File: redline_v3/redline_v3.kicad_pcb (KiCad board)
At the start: 2 copper layers, 89.1 x 94.5 mm, 67 parts, among them J1 Conn_01x10_Socket, J2 Conn_01x10_Socket

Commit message: V3 with Gia layout
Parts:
- moved D23 79.7 mm to (218.7, 137.6), turned to 90 degrees
- moved D33 73.0 mm to (216.6, 137.5), turned to 90 degrees
- moved D24 71.7 mm to (213.9, 133.2), turned to 90 degrees
- moved J2 71.1 mm to (232.4, 101.7), turned to 0 degrees
- moved D17 66.1 mm to (170.4, 67.9), turned to 0 degrees
- moved D12 66.1 mm to (190.6, 91.4), turned to -90 degrees
- moved D11 65.6 mm to (185.7, 86.6), turned to 0 degrees
- moved D21 65.5 mm to (185.7, 84.7)
- moved D22 65.2 mm to (192.6, 91.4), turned to -90 degrees
- moved D34 64.9 mm to (211.6, 133.2), turned to 90 degrees
- moved D1 63.9 mm to (155.1, 134.1)
- moved D2 63.7 mm to (155.0, 135.9)
- moved D18 61.2 mm to (174.1, 72.5), turned to 0 degrees
- moved D42 59.1 mm to (190.5, 94.9), turned to 90 degrees
- moved D7 58.7 mm to (170.4, 69.8), turned to 0 degrees
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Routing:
- net /1: track 0.00 -> 211.9 mm
- net /0: track 39.0 -> 236.2 mm
- net /2: track 0.00 -> 103.5 mm
- net /3: track 0.00 -> 88.5 mm
- net Net-(D1-K): track 57.1 -> 0.00 mm
- net /8: track 0.00 -> 32.9 mm
- net /9: track 39.2 -> 8.06 mm
- net /5: track 44.0 -> 73.3 mm
- net Net-(D10-K): track 28.8 -> 0.00 mm
- net Net-(D43-K): track 4.46 -> 31.8 mm
- net Net-(D23-K): track 35.0 -> 8.78 mm, vias 4 -> 0
- net /4: track 41.5 -> 65.3 mm
- net /6: track 55.0 -> 76.3 mm
- net /7: track 37.4 -> 55.5 mm
- net Net-(D33-K): track 4.57 -> 17.8 mm
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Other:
- board size 89.1 x 94.5 mm -> 104.8 x 108.8 mm

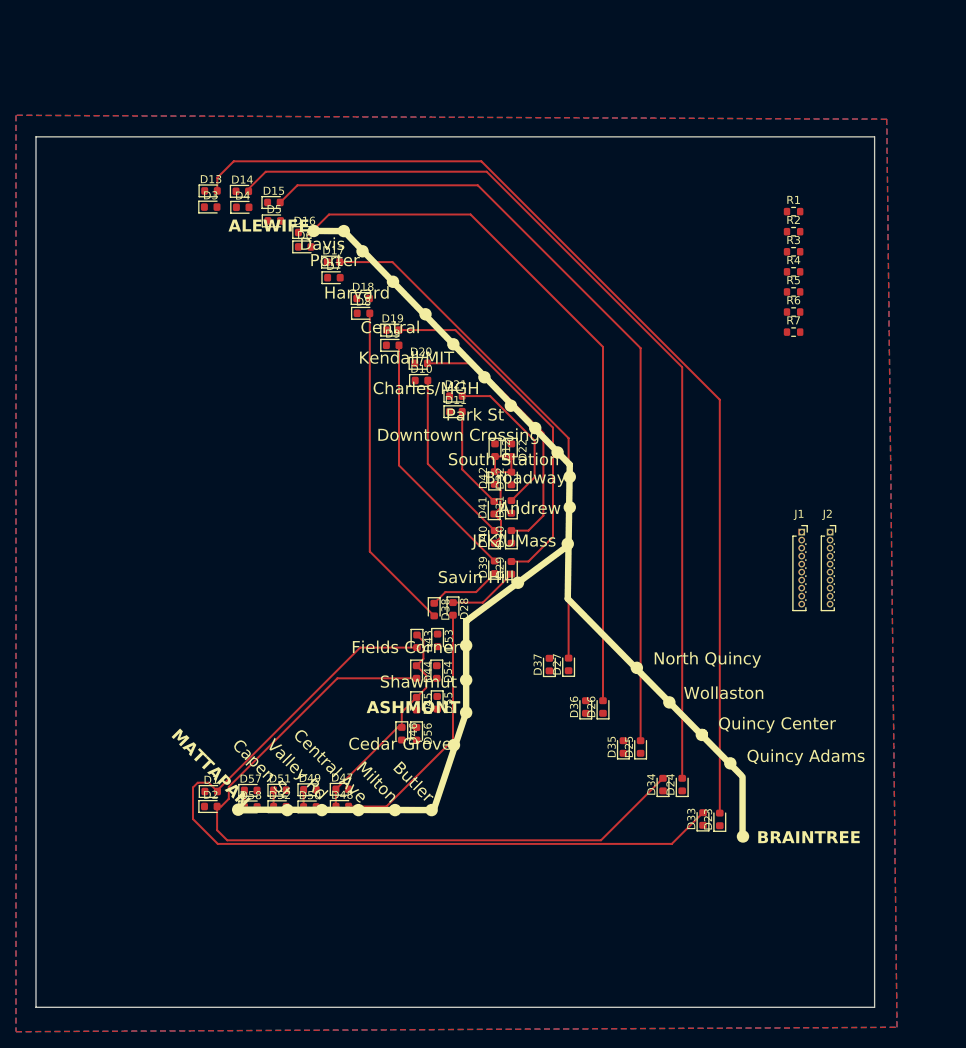
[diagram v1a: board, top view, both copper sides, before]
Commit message: remove old silkscreen
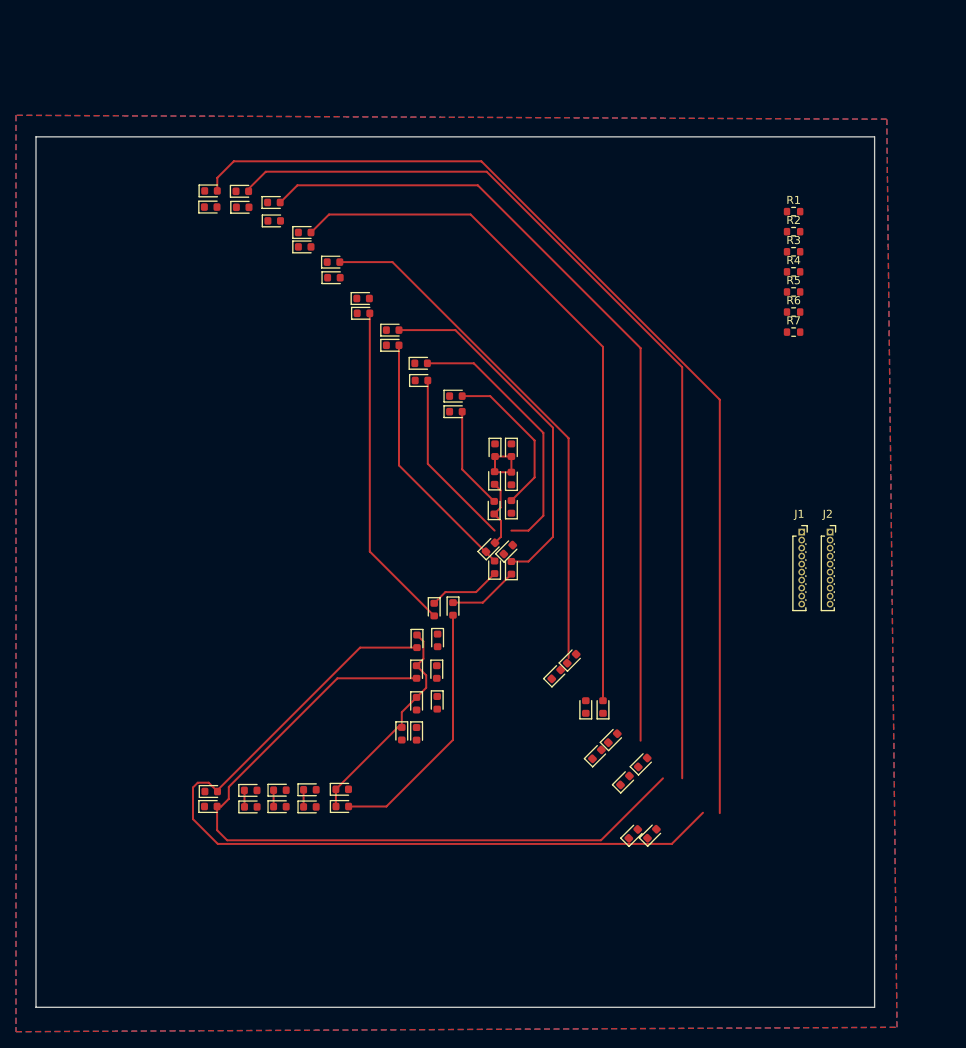
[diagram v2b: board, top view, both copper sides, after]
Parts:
- moved D33 8.91 mm to (207.8, 139.4), turned to 45 degrees
- moved D23 8.67 mm to (210.2, 139.4), turned to 45 degrees
- moved D24 5.66 mm to (209.0, 130.4), turned to 45 degrees
- moved D34 4.78 mm to (206.8, 132.7), turned to 45 degrees
- moved D25 3.65 mm to (205.3, 127.4), turned to 45 degrees
- moved D35 3.43 mm to (203.3, 129.4), turned to 45 degrees
- moved D30 1.63 mm to (192.2, 103.8), turned to 45 degrees
- moved D37 1.49 mm to (198.2, 119.4), turned to 45 degrees
- moved D40 1.39 mm to (190.0, 103.5), turned to 45 degrees
- moved D27 0.81 mm to (200.1, 117.5), turned to 45 degrees
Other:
- board text removed: "ALEWIFE"
- board text removed: "ASHMONT"
- board text removed: "Andrew"
- board text removed: "BRAINTREE"
- board text removed: "Broadway"
- board text removed: "Butler"
- board text removed: "Capen St"
- board text removed: "Cedar Grove"
- board text removed: "Central"
- board text removed: "Central Ave"
- board text removed: "Charles/MGH"
- board text removed: "Davis"
- board text removed: "Downtown Crossing"
- board text removed: "Fields Corner"
- board text removed: "Harvard"
- board text removed: "JFK/UMass"
- board text removed: "Kendall/MIT"
- board text removed: "MATTAPAN"
- board text removed: "Milton"
- board text removed: "North Quincy"
- board text removed: "Park St"
- board text removed: "Porter"
- board text removed: "Quincy Adams"
- board text removed: "Quincy Center"
- board text removed: "Savin Hill"
- board text removed: "Shawmut"
- board text removed: "South Station"
- board text removed: "Valley Rd"
- board text removed: "Wollaston"

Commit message: fix led locations
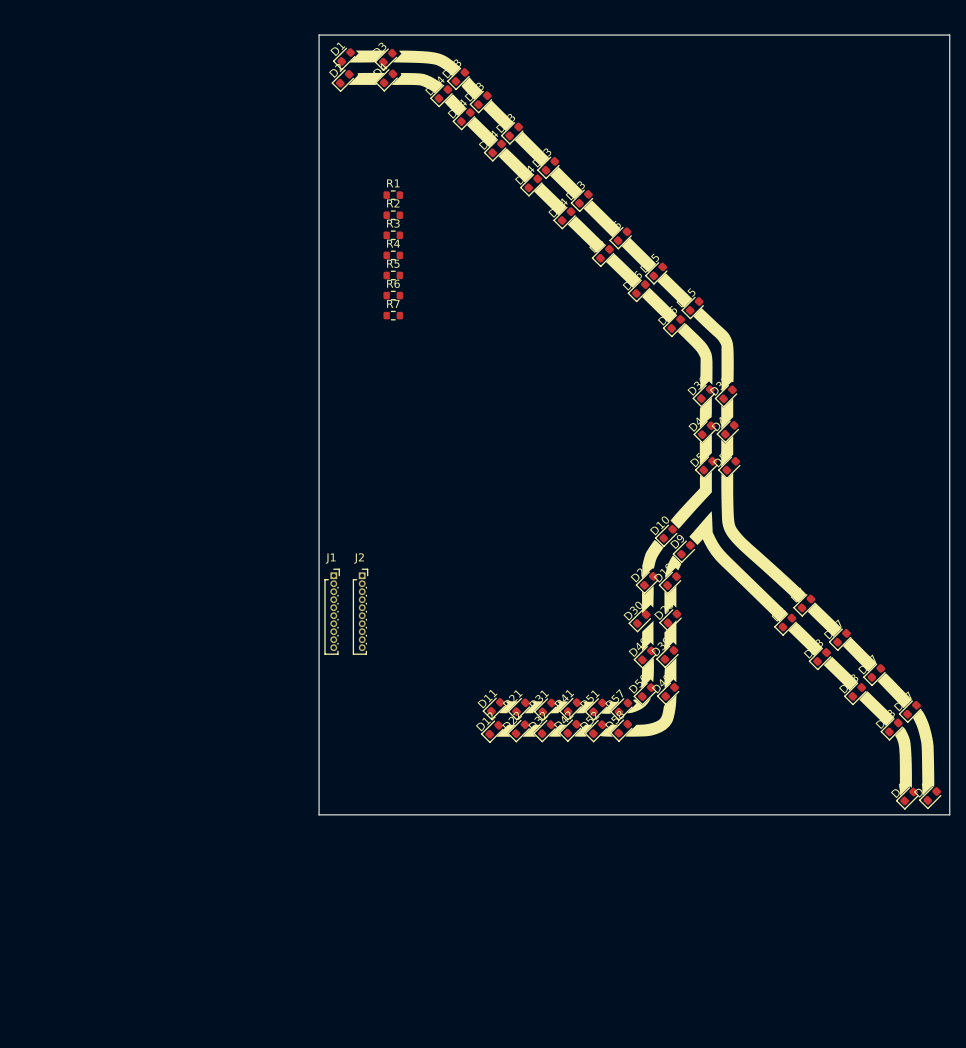
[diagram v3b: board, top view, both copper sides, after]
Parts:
- added G***: LOGO, silkscreen:redline_nolabels, F.Cu at (209.2, 87.9)
- moved D23 94.1 mm to (189.0, 47.7)
- moved D1 93.4 mm to (171.9, 42.3), turned to 45 degrees
- moved D2 92.5 mm to (171.8, 45.0), turned to 45 degrees
- moved D33 89.1 mm to (192.9, 51.6)
- moved D24 83.6 mm to (186.9, 49.8)
- moved D34 80.6 mm to (190.8, 53.7)
- moved D17 79.0 mm to (233.9, 114.9), turned to 45 degrees
- moved D47 73.8 mm to (245.2, 134.6), turned to 45 degrees
- moved D18 72.8 mm to (231.4, 117.3), turned to 45 degrees
- moved D7 71.8 mm to (229.5, 110.6), turned to 45 degrees
- moved D48 70.9 mm to (242.3, 134.7), turned to 45 degrees
- moved D8 65.6 mm to (227.1, 113.0), turned to 45 degrees
- moved D44 62.8 mm to (195.3, 58.1), turned to 45 degrees
- moved D43 61.7 mm to (197.5, 55.9), turned to 45 degrees
- moved D38 59.3 mm to (240.4, 126.1), turned to 45 degrees
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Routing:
- net /0: track 236.2 -> 0.00 mm
- net /1: track 211.9 -> 0.00 mm
- net /2: track 103.5 -> 0.00 mm
- net /3: track 88.5 -> 0.00 mm
- net /6: track 76.3 -> 0.00 mm
- net /5: track 73.3 -> 0.00 mm
- net /4: track 65.3 -> 0.00 mm
- net /7: track 55.5 -> 0.00 mm
- net /8: track 32.9 -> 0.00 mm
- net Net-(D43-K): track 31.8 -> 0.00 mm
- net Net-(D33-K): track 17.8 -> 0.00 mm
- net Net-(D23-K): track 8.78 -> 0.00 mm
- net /9: track 8.06 -> 0.00 mm
- net Net-(D53-K): track 2.07 -> 0.00 mm
- removed copper zone on B.Cu, net GND
- removed copper zone on F.Cu, net GND
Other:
- board size 104.8 x 108.8 mm -> 78.8 x 97.5 mm

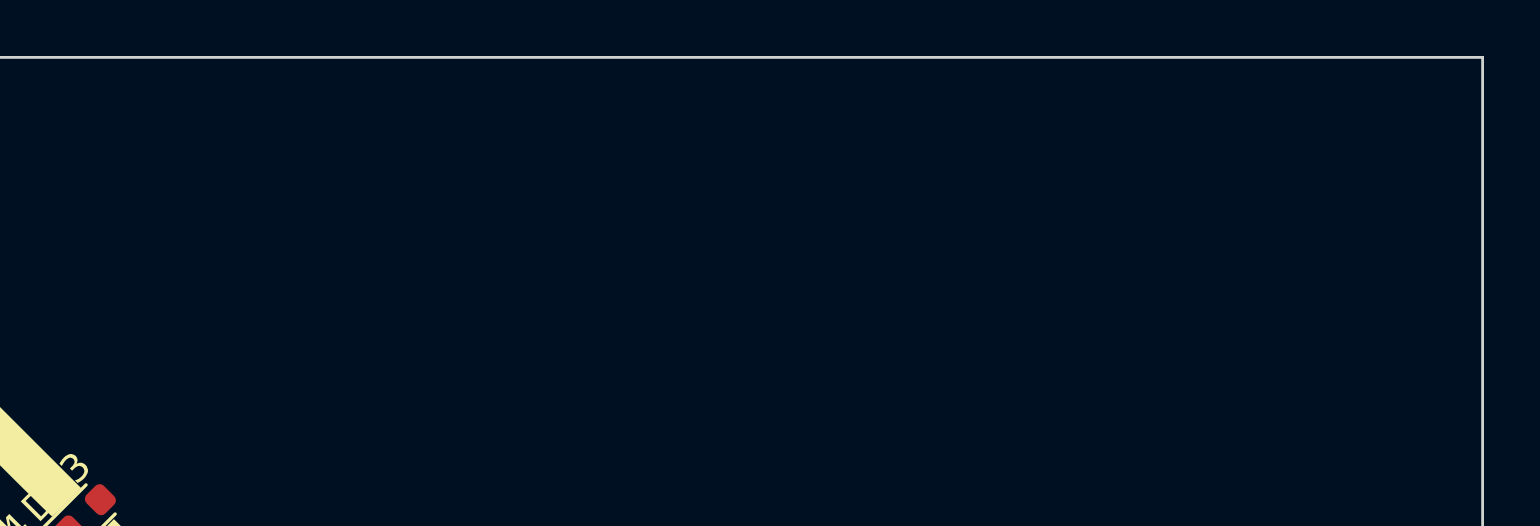
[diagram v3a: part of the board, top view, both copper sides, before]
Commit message: add mbta sign
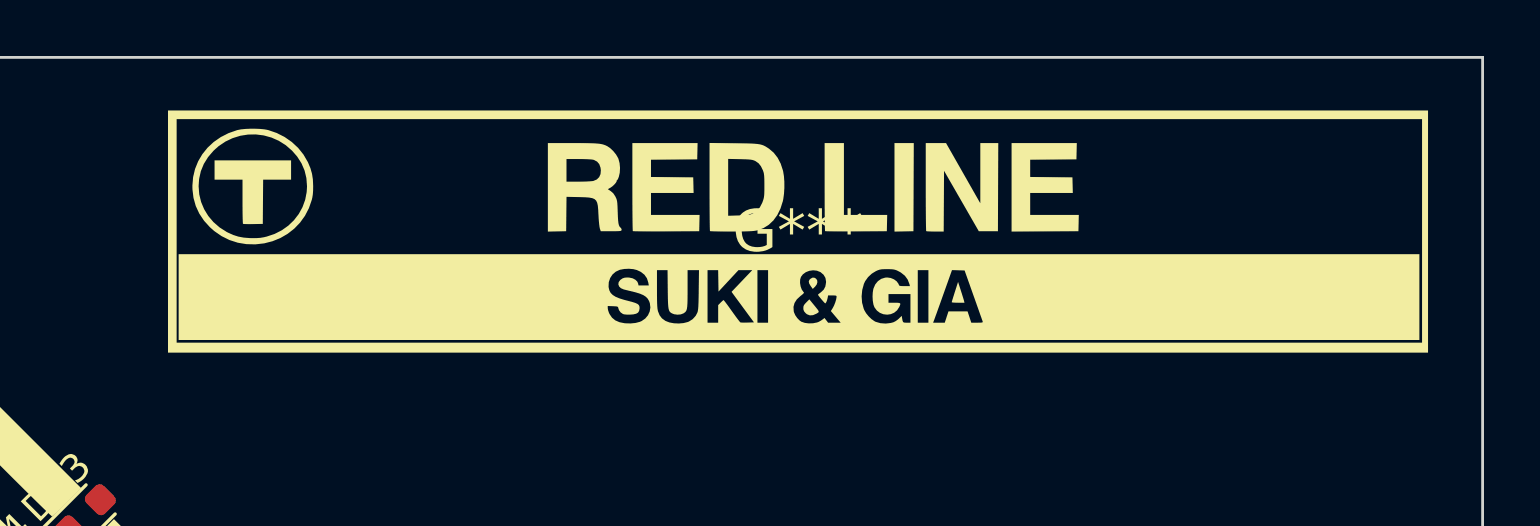
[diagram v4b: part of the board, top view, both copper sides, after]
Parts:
- added G***: LOGO, silkscreen:sign, F.Cu at (222.9, 45.7)

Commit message: traces all done
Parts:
- removed the G*** at (222.9, 45.7)
- removed J1, J2: Conn_01x10_Socket, Connector_PinSocket_1.00mm:PinSocket_1x10_P1.00mm_Vertical
- added C1: 10nF, Capacitor_SMD:C_0603_1608Metric, F.Cu at (220.5, 77.5)
- added C2: 3.3nF, Capacitor_SMD:C_0603_1608Metric, F.Cu at (223.0, 76.8)
- added C3: C_1uF, footprints:C_0603_1608Metric, F.Cu at (231.2, 82.8)
- added C4: C_1uF, footprints:C_0603_1608Metric, F.Cu at (227.7, 85.8)
- added J4: 48037-0001, custom_library:MOLEX_USB_conn, F.Cu at (216.2, 55.0)
- added R8: R_US, Resistor_SMD:R_0603_1608Metric, F.Cu at (223.1, 78.2)
- added U1: ESP32, Package_DFN_QFN:QFN-48-1EP_8x8mm_P0.5mm_EP6.2x6.2mm, F.Cu at (215.0, 81.5)
- added U2: MCP1702T-3302E_MB, custom_library:MCP1702T, F.Cu at (228.0, 82.8)
- moved D23 110.0 mm to (219.5, 153.3)
- moved D33 104.5 mm to (216.6, 153.3)
- moved D1 99.8 mm to (165.3, 141.8)
- moved D2 99.5 mm to (165.5, 144.3)
- moved D24 97.1 mm to (217.4, 142.0)
- moved D34 93.8 mm to (215.1, 144.3)
- moved R5 88.4 mm to (213.5, 150.5), turned to 90 degrees
- moved R1 81.7 mm to (161.5, 139.6), turned to 90 degrees
- moved D17 80.1 mm to (167.8, 69.6)
- moved D44 78.2 mm to (184.2, 135.4)
- moved R6 77.0 mm to (174.7, 149.0), turned to 180 degrees
- moved D43 76.1 mm to (184.1, 130.8)
- moved R7 74.9 mm to (169.0, 149.0), turned to 180 degrees
- moved D7 74.7 mm to (165.5, 71.9)
- moved D54 74.3 mm to (187.0, 135.4)
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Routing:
- net /1: track 0.00 -> 298.4 mm, vias 0 -> 15
- net /0: track 0.00 -> 284.1 mm, vias 0 -> 4
- net /2: track 0.00 -> 255.7 mm, vias 0 -> 11
- net /A: track 0.00 -> 188.6 mm, vias 0 -> 4
- net /4: track 0.00 -> 186.6 mm, vias 0 -> 11
- net /5: track 0.00 -> 175.5 mm, vias 0 -> 18
- net /3: track 0.00 -> 157.8 mm, vias 0 -> 11
- net /6: track 0.00 -> 150.6 mm, vias 0 -> 13
- net /G: track 0.00 -> 135.6 mm, vias 0 -> 2
- net /F: track 0.00 -> 130.4 mm, vias 0 -> 4
- net /7: track 0.00 -> 128.4 mm, vias 0 -> 12
- net /9: track 0.00 -> 120.0 mm, vias 0 -> 12
- net /8: track 0.00 -> 111.2 mm, vias 0 -> 8
- net /B: track 0.00 -> 104.3 mm, vias 0 -> 2
- net /E: track 0.00 -> 89.1 mm, vias 0 -> 2
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- added copper zone on B.Cu, net (none)
- added copper zone on F.Cu, net (none)
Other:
- board size 78.8 x 97.5 mm -> 104.8 x 108.8 mm

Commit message: add station names
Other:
- board text added: "Alewife"
- board text added: "Andrew"
- board text added: "Ashmont"
- board text added: "Braintree"
- board text added: "Broadway"
- board text added: "Butler"
- board text added: "Capen St"
- board text added: "Cedar Grove"
- board text added: "Central"
- board text added: "Central Ave"
- board text added: "Charles/MGH"
- board text added: "Davis"
- board text added: "Downtown Crossing"
- board text added: "Fields Corner"
- board text added: "Harvard"
- board text added: "JFK/UMass"
- board text added: "Kendall/MIT"
- board text added: "Mattapan"
- board text added: "Milton"
- board text added: "North Quincy"
- board text added: "Park St"
- board text added: "Porter"
- board text added: "Quincy Adams"
- board text added: "Quincy Center"
- board text added: "Savin Hill"
- board text added: "Shawmut"
- board text added: "South Station"
- board text added: "Valley Rd"
- board text added: "Wollaston"
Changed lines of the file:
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@@
   (gr_rect (start 133.175 52.243519) (end 238 161.05)
     (stroke (width 0.05) (type default)) (fill none) (layer "Edge.Cuts"))
+  (gr_text "Broadway" (at 195.93 103.45) (layer "F.SilkS")
+    (effects (font (size 1 1) (thickness 0.15)) (justify left bottom))
+  )
+  (gr_text "JFK/UMass" (at 195.77 112.49) (layer "F.SilkS")
+    (effects (font (size 1 1) (thickness 0.15)) (justify left bottom))
+  )
+  (gr_text "Mattapan\n" (at 164.89 147.11 -45) (layer "F.SilkS")
+    (effects (font (size 1 1) (thickness 0.15)) (justify left bottom))
+  )
+  (gr_text "Central Ave\n" (at 174.39 147.35 -45) (layer "F.SilkS")
+    (effects (font (size 1 1) (thickness 0.15)) (justify left bottom))
+  )
+  (gr_text "Charles/MGH" (at 177.46 77.14) (layer "F.SilkS")
+    (effects (font (size 1 1) (thickness 0.15)) (justify left bottom))
+  )
+  (gr_text "Valley Rd" (at 171.15 147.33 -45) (layer "F.SilkS")
+    (effects (font (size 1 1) (thickness 0.15)) (justify left bottom))
+  )
+  (gr_text "Butler\n" (at 180.83 147.32 -45) (layer "F.SilkS")
+    (effects (font (size 1 1) (thickness 0.15)) (justify left bottom))
+  )
+  (gr_text "Cedar Grove\n" (at 188.19 141.31 -45) (layer "F.SilkS")
+    (effects (font (size 1 1) (thickness 0.15)) (justify left bottom))
+  )
+  (gr_text "Fields Corner" (at 172.79 125.65) (layer "F.SilkS")
+    (effects (font (size 1 1) (thickness 0.15)) (justify left bottom))
+  )
+  (gr_text "North Quincy\n" (at 205.15 127.83) (layer "F.SilkS")
+    (effects (font (size 1 1) (thickness 0.15)) (justify left bottom))
+  )
+  (gr_text "Central" (at 168.87 68.54) (layer "F.SilkS")
+    (effects (font (size 1 1) (thickness 0.15)) (justify left bottom))
+  )
+  (gr_text "Wollaston\n" (at 209.62 132.06) (layer "F.SilkS")
+    (effects (font (size 1 1) (thickness 0.15)) (justify left bottom))
+  )
+  (gr_text "Park St" (at 182.12 81.98) (layer "F.SilkS")
+    (effects (font (size 1 1) (thickness 0.15)) (justify left bottom))
+  )
+  (gr_text "Andrew" (at 195.97 107.96) (layer "F.SilkS")
+    (effects (font (size 1 1) (thickness 0.15)) (justify left bottom))
+  )
+  (gr_text "Davis\n" (at 148.15 56.88 -45) (layer "F.SilkS")
+    (effects (font (size 1 1) (thickness 0.15)) (justify left bottom))
+  )
+  (gr_text "South Station" (at 191.11 90.69) (layer "F.SilkS")
+    (effects (font (size 1 1) (thickness 0.15)) (justify left bottom))
+  )
+  (gr_text "Downtown Crossing" (at 186.67 86.32) (layer "F.SilkS")
+    (effects (font (size 1 1) (thickness 0.15)) (justify left bottom))
+  )
+  (gr_text "Milton\n" (at 177.51 147.38 -45) (layer "F.SilkS")
+    (effects (font (size 1 1) (thickness 0.15)) (justify left bottom))
+  )
+  (gr_text "Quincy Center\n" (at 213.99 136.44) (layer "F.SilkS")
+    (effects (font (size 1 1) (thickness 0.15)) (justify left bottom))
+  )
+  (gr_text "Kendall/MIT" (at 173.19 73.08) (layer "F.SilkS")
+    (effects (font (size 1 1) (thickness 0.15)) (justify left bottom))
+  )
+  (gr_text "Braintree" (at 221.21 154.05) (layer "F.SilkS")
+    (effects (font (size 1 1) (thickness 0.15)) (justify left bottom))
+  )
+  (gr_text "Porter" (at 162.13 61.82) (layer "F.SilkS")
+    (effects (font (size 1 1) (thickness 0.15)) (justify left bottom))
+  )
+  (gr_text "Alewife" (at 141.5 56.16 -45) (layer "F.SilkS")
+    (effects (font (size 1 1) (thickness 0.15)) (justify left bottom))
+  )
+  (gr_text "Harvard" (at 165 64.64) (layer "F.SilkS")
+    (effects (font (size 1 1) (thickness 0.15)) (justify left bottom))
+  )
+  (gr_text "Savin Hill" (at 178.31 119.48) (layer "F.SilkS")
+    (effects (font (size 1 1) (thickness 0.15)) (justify left bottom))
+  )
+  (gr_text "Quincy Adams\n" (at 218.44 140.94) (layer "F.SilkS")
+    (effects (font (size 1 1) (thickness 0.15)) (justify left bottom))
+  )
+  (gr_text "Capen St" (at 167.86 147.35 -45) (layer "F.SilkS")
+    (effects (font (size 1 1) (thickness 0.15)) (justify left bottom))
+  )
+  (gr_text "Shawmut\n" (at 176.02 130.75) (layer "F.SilkS")
+    (effects (font (size 1 1) (thickness 0.15)) (justify left bottom))
+  )
+  (gr_text "Ashmont\n" (at 176.23 135.34) (layer "F.SilkS")
+    (effects (font (size 1 1) (thickness 0.15)) (justify left bottom))
+  )
   (segment (start 152.523694 60.036306) (end 153.636306 60.036306) (width 0.25) (layer "F.Cu") (net 1))
   (segment (start 144.2 109) (end 163.2 128) (width 0.25) (layer "F.Cu") (net 1))

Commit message: add mbta sign
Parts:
- added G***: LOGO, silkscreen:sign, F.Cu at (209.1, 66.9)
- moved R7 10.0 mm to (176.7, 155.5), turned to 135 degrees
- moved R4 9.16 mm to (220.8, 130.4), turned to -135 degrees
- moved R6 6.19 mm to (177.6, 154.5), turned to 135 degrees
- moved R3 5.63 mm to (169.6, 62.6), turned to 180 degrees
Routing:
- net Net-(D53-K): track 44.2 -> 54.5 mm
- net /G: track 135.6 -> 125.4 mm
- net /D: track 59.0 -> 48.9 mm
- net Net-(D23-K): track 79.3 -> 87.9 mm
- net /F: track 130.4 -> 123.2 mm
- net /C: track 68.9 -> 61.8 mm
- net Net-(D43-K): track 41.7 -> 48.3 mm
- net Net-(D13-K): track 61.2 -> 66.0 mm
